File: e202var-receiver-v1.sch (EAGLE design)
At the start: 46 parts, among them P10 10k, Q1 BC237A/EQUIV, Q2 BC237A/EQUIV, U1 MC7809, U2 TLE2426, U3 LM386

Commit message: Added BOM.
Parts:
- removed JP1: 9V, SparkFun-Connectors:M02LOCK
- removed JP3: HEADPHONES, SparkFun-Connectors:AUDIO-JACK2.5MM
- added J1: 9V, SparkFun-Connectors:POWER_JACKPTH
- added J3: HEADPHONES, SparkFun-Connectors:AUDIO-JACK2KIT
- D3: value BLUE -> 3.2V BLUE
- renumbered HPF to JUMP1, JP2 to J2
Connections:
- net GND: now also J1.GND, J1.GNDBREAK, J3.RING, J3.RSH, J3.SLEEVE; no longer JP1.2, JP3.SLEEVE
- net N$1: now also J1.PWR; no longer JP1.1
- net N$25: now also J3.TIP, J3.TSH; no longer JP3.LEFT, JP3.RIGHT
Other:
- note added: "VOLUME"
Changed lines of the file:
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@@
 <parts>
 <part name="D1" library="max-viz" deviceset="S5BC-13" device="" value="1N4001"/>
-<part name="JP1" library="SparkFun-Connectors" deviceset="M02" device="LOCK" value="9V"/>
-<part name="JP2" library="SparkFun-Connectors" deviceset="M02" device="LOCK" value="ON/OFF"/>
+<part name="J2" library="SparkFun-Connectors" deviceset="M02" device="LOCK" value="ON/OFF"/>
 <part name="U1" library="SparkFun-PowerIC" deviceset="V_REG_LD1117VXX" device="" value="MC7809"/>
 <part name="D2" library="max-viz" deviceset="S5BC-13" device="" value="1N4001"/>
@@
 <part name="R4" library="SparkFun-Passives" deviceset="RESISTOR" device="EZ" value="3.3k"/>
 <part name="C16" library="SparkFun-Capacitors" deviceset="CAP" device="KIT" value="4.7n"/>
-<part name="HPF" library="SparkFun-Retired" deviceset="JUMPER-2" device="PTH_LOCK" value="HPF"/>
+<part name="JUMP1" library="SparkFun-Retired" deviceset="JUMPER-2" device="PTH_LOCK" value="HPF"/>
 <part name="U$7" library="max-viz" deviceset="GND" device=""/>
 <part name="U$8" library="max-viz" deviceset="GND" device=""/>
@@
 <part name="U$9" library="max-viz" deviceset="GND" device=""/>
 <part name="R12" library="SparkFun-Passives" deviceset="RESISTOR" device="EZ" value="2.2k"/>
-<part name="D3" library="SparkFun-LED" deviceset="LTE-302" device="" value="BLUE"/>
+<part name="D3" library="SparkFun-LED" deviceset="LTE-302" device="" value="3.2V BLUE"/>
 <part name="U$10" library="max-viz" deviceset="GND" device=""/>
 <part name="R9" library="SparkFun-Passives" deviceset="RESISTOR" device="EZ" value="33"/>
 <part name="R7" library="SparkFun-Passives" deviceset="RESISTOR" device="EZ" value="10"/>
 <part name="C9" library="SparkFun-Passives" deviceset="CAP" device="PTH1" value="100u"/>
-<part name="JP3" library="SparkFun-Connectors" deviceset="AUDIO-JACK" device="2.5MM" value="HEADPHONES"/>
+<part name="J3" library="SparkFun-Connectors" deviceset="AUDIO-JACK2" device="KIT" value="HEADPHONES"/>
 <part name="C10" library="SparkFun-Capacitors" deviceset="CAP" device="KIT" value="10n"/>
 <part name="U$11" library="max-viz" deviceset="GND" device=""/>
@@
 <part name="U$13" library="max-viz" deviceset="GND" device=""/>
 <part name="25-OCT-2015" library="max-viz" deviceset="FRAME-INFOBOX-WICKER" device="" value="VLF Natural Radio Receiver v1"/>
+<part name="J1" library="SparkFun-Connectors" deviceset="POWER_JACK" device="PTH" value="9V"/>
 </parts>
 <sheets>
@@
 <wire x1="238.76" y1="20.32" x2="238.76" y2="66.04" width="0.1524" layer="94"/>
 <frame x1="0" y1="0" x2="335.28" y2="182.88" columns="8" rows="5" layer="94"/>
+<text x="218.44" y="93.98" size="1.778" layer="97" rot="R90">VOLUME</text>
 </plain>
 <instances>
 <instance part="D1" gate="G$1" x="38.1" y="165.1" rot="R270"/>
-<instance part="JP1" gate="G$1" x="15.24" y="109.22" rot="MR180"/>
-<instance part="JP2" gate="G$1" x="15.24" y="129.54" rot="MR180"/>
+<instance part="J2" gate="G$1" x="15.24" y="129.54" rot="MR180"/>
 <instance part="U1" gate="G$1" x="63.5" y="149.86"/>
 <instance part="D2" gate="G$1" x="48.26" y="149.86" rot="R270"/>
@@
 <instance part="R4" gate="G$1" x="144.78" y="96.52"/>
 <instance part="C16" gate="G$1" x="137.16" y="83.82"/>
-<instance part="HPF" gate="A" x="147.32" y="86.36" rot="R270"/>
+<instance part="JUMP1" gate="A" x="147.32" y="86.36" rot="R270"/>
 <instance part="U$7" gate="G$1" x="154.94" y="129.54"/>
 <instance part="U$8" gate="G$1" x="162.56" y="99.06"/>
@@
 <instance part="R7" gate="G$1" x="276.86" y="91.44" rot="R90"/>
 <instance part="C9" gate="G$1" x="297.18" y="99.06" rot="R90"/>
-<instance part="JP3" gate="G$1" x="317.5" y="96.52" rot="R180"/>
+<instance part="J3" gate="G$1" x="317.5" y="96.52" rot="R180"/>
 <instance part="C10" gate="G$1" x="276.86" y="78.74"/>
 <instance part="U$11" gate="G$1" x="33.02" y="142.24"/>
@@
 <instance part="U$13" gate="G$1" x="241.3" y="119.38"/>
 <instance part="25-OCT-2015" gate="G$1" x="66.04" y="22.86"/>
+<instance part="J1" gate="G$1" x="20.32" y="101.6"/>
 </instances>
 <busses>
@@
 <net name="N$1" class="0">
 <segment>
-<pinref part="JP1" gate="G$1" pin="1"/>
 <wire x1="22.86" y1="109.22" x2="25.4" y2="109.22" width="0.1524" layer="91"/>
 <wire x1="25.4" y1="109.22" x2="25.4" y2="127" width="0.1524" layer="91"/>
-<pinref part="JP2" gate="G$1" pin="2"/>
+<pinref part="J2" gate="G$1" pin="2"/>
 <wire x1="25.4" y1="127" x2="22.86" y2="127" width="0.1524" layer="91"/>
+<pinref part="J1" gate="G$1" pin="PWR"/>
 </segment>
 </net>
 <net name="N$2" class="0">
 <segment>
-<pinref part="JP2" gate="G$1" pin="1"/>
+<pinref part="J2" gate="G$1" pin="1"/>
 <wire x1="22.86" y1="129.54" x2="25.4" y2="129.54" width="0.1524" layer="91"/>
 <wire x1="25.4" y1="129.54" x2="25.4" y2="165.1" width="0.1524" layer="91"/>
@@
 <pinref part="C16" gate="G$1" pin="2"/>
 <wire x1="137.16" y1="73.66" x2="137.16" y2="78.74" width="0.1524" layer="91"/>
-<pinref part="HPF" gate="A" pin="2"/>
+<pinref part="JUMP1" gate="A" pin="2"/>
 <wire x1="137.16" y1="78.74" x2="137.16" y2="81.28" width="0.1524" layer="91"/>
 <wire x1="137.16" y1="78.74" x2="147.32" y2="78.74" width="0.1524" layer="91"/>
@@
 <wire x1="114.3" y1="86.36" x2="114.3" y2="81.28" width="0.1524" layer="91"/>
 <junction x="114.3" y="86.36"/>
-<pinref part="JP1" gate="G$1" pin="2"/>
 <wire x1="22.86" y1="106.68" x2="25.4" y2="106.68" width="0.1524" layer="91"/>
-<wire x1="25.4" y1="106.68" x2="25.4" y2="81.28" width="0.1524" layer="91"/>
+<wire x1="25.4" y1="106.68" x2="25.4" y2="104.14" width="0.1524" layer="91"/>
+<wire x1="25.4" y1="104.14" x2="25.4" y2="81.28" width="0.1524" layer="91"/>
 <wire x1="114.3" y1="81.28" x2="68.58" y2="81.28" width="0.1524" layer="91"/>
 <pinref part="LAMP" gate="G$1" pin="2"/>
@@
 <wire x1="25.4" y1="81.28" x2="25.4" y2="78.74" width="0.1524" layer="91"/>
 <junction x="25.4" y="81.28"/>
+<pinref part="J1" gate="G$1" pin="GNDBREAK"/>
+<pinref part="J1" gate="G$1" pin="GND"/>
+<wire x1="22.86" y1="104.14" x2="25.4" y2="104.14" width="0.1524" layer="91"/>
+<junction x="25.4" y="104.14"/>
 </segment>
 <segment>
@@
 <wire x1="251.46" y1="83.82" x2="231.14" y2="83.82" width="0.1524" layer="91"/>
 <junction x="231.14" y="83.82"/>
-<pinref part="JP3" gate="G$1" pin="SLEEVE"/>
-<wire x1="312.42" y1="93.98" x2="309.88" y2="93.98" width="0.1524" layer="91"/>
-<wire x1="309.88" y1="93.98" x2="309.88" y2="68.58" width="0.1524" layer="91"/>
-<wire x1="309.88" y1="68.58" x2="276.86" y2="68.58" width="0.1524" layer="91"/>
+<wire x1="297.18" y1="91.44" x2="297.18" y2="68.58" width="0.1524" layer="91"/>
+<wire x1="297.18" y1="68.58" x2="276.86" y2="68.58" width="0.1524" layer="91"/>
 <wire x1="276.86" y1="68.58" x2="261.62" y2="68.58" width="0.1524" layer="91"/>
 <wire x1="261.62" y1="68.58" x2="251.46" y2="68.58" width="0.1524" layer="91"/>
@@
 <wire x1="276.86" y1="76.2" x2="276.86" y2="68.58" width="0.1524" layer="91"/>
 <junction x="276.86" y="68.58"/>
+<pinref part="J3" gate="G$1" pin="SLEEVE"/>
+<wire x1="312.42" y1="91.44" x2="302.26" y2="91.44" width="0.1524" layer="91"/>
+<pinref part="J3" gate="G$1" pin="RSH"/>
+<wire x1="302.26" y1="91.44" x2="297.18" y2="91.44" width="0.1524" layer="91"/>
+<wire x1="312.42" y1="96.52" x2="302.26" y2="96.52" width="0.1524" layer="91"/>
+<wire x1="302.26" y1="96.52" x2="302.26" y2="93.98" width="0.1524" layer="91"/>
+<junction x="302.26" y="91.44"/>
+<pinref part="J3" gate="G$1" pin="RING"/>
+<wire x1="302.26" y1="93.98" x2="302.26" y2="91.44" width="0.1524" layer="91"/>
+<wire x1="312.42" y1="93.98" x2="302.26" y2="93.98" width="0.1524" layer="91"/>
+<junction x="302.26" y="93.98"/>
 </segment>
 <segment>
@@
 <wire x1="137.16" y1="96.52" x2="137.16" y2="91.44" width="0.1524" layer="91"/>
 <pinref part="C16" gate="G$1" pin="1"/>
-<pinref part="HPF" gate="A" pin="1"/>
+<pinref part="JUMP1" gate="A" pin="1"/>
 <wire x1="137.16" y1="91.44" x2="137.16" y2="88.9" width="0.1524" layer="91"/>
 <wire x1="137.16" y1="91.44" x2="147.32" y2="91.44" width="0.1524" layer="91"/>
@@
 <segment>
 <pinref part="C9" gate="G$1" pin="2"/>
-<pinref part="JP3" gate="G$1" pin="LEFT"/>
-<wire x1="299.72" y1="99.06" x2="309.88" y2="99.06" width="0.1524" layer="91"/>
-<pinref part="JP3" gate="G$1" pin="RIGHT"/>
-<wire x1="309.88" y1="99.06" x2="312.42" y2="99.06" width="0.1524" layer="91"/>
-<wire x1="312.42" y1="96.52" x2="309.88" y2="96.52" width="0.1524" layer="91"/>
-<wire x1="309.88" y1="96.52" x2="309.88" y2="99.06" width="0.1524" layer="91"/>
-<junction x="309.88" y="99.06"/>
-</segment>
-</net>
+<wire x1="299.72" y1="99.06" x2="302.26" y2="99.06" width="0.1524" layer="91"/>
+<pinref part="J3" gate="G$1" pin="TSH"/>
+<wire x1="312.42" y1="99.06" x2="302.26" y2="99.06" width="0.1524" layer="91"/>
+<junction x="302.26" y="99.06"/>
+<pinref part="J3" gate="G$1" pin="TIP"/>
+<wire x1="312.42" y1="101.6" x2="302.26" y2="101.6" width="0.1524" layer="91"/>
+<wire x1="302.26" y1="101.6" x2="302.26" y2="99.06" width="0.1524" layer="91"/>
+</segment>
+</net>

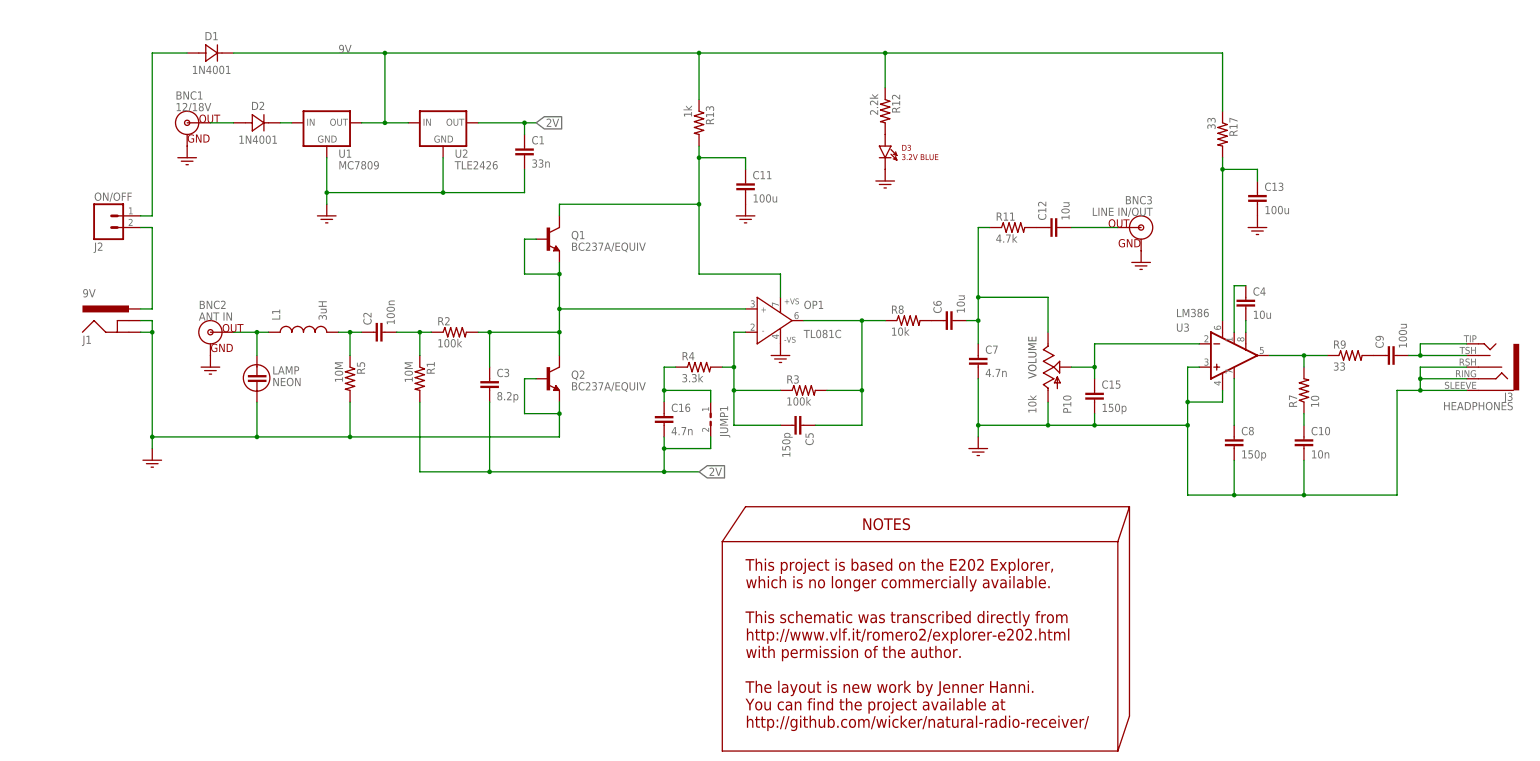
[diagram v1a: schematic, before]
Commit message: Added e202var library and clean schematic.
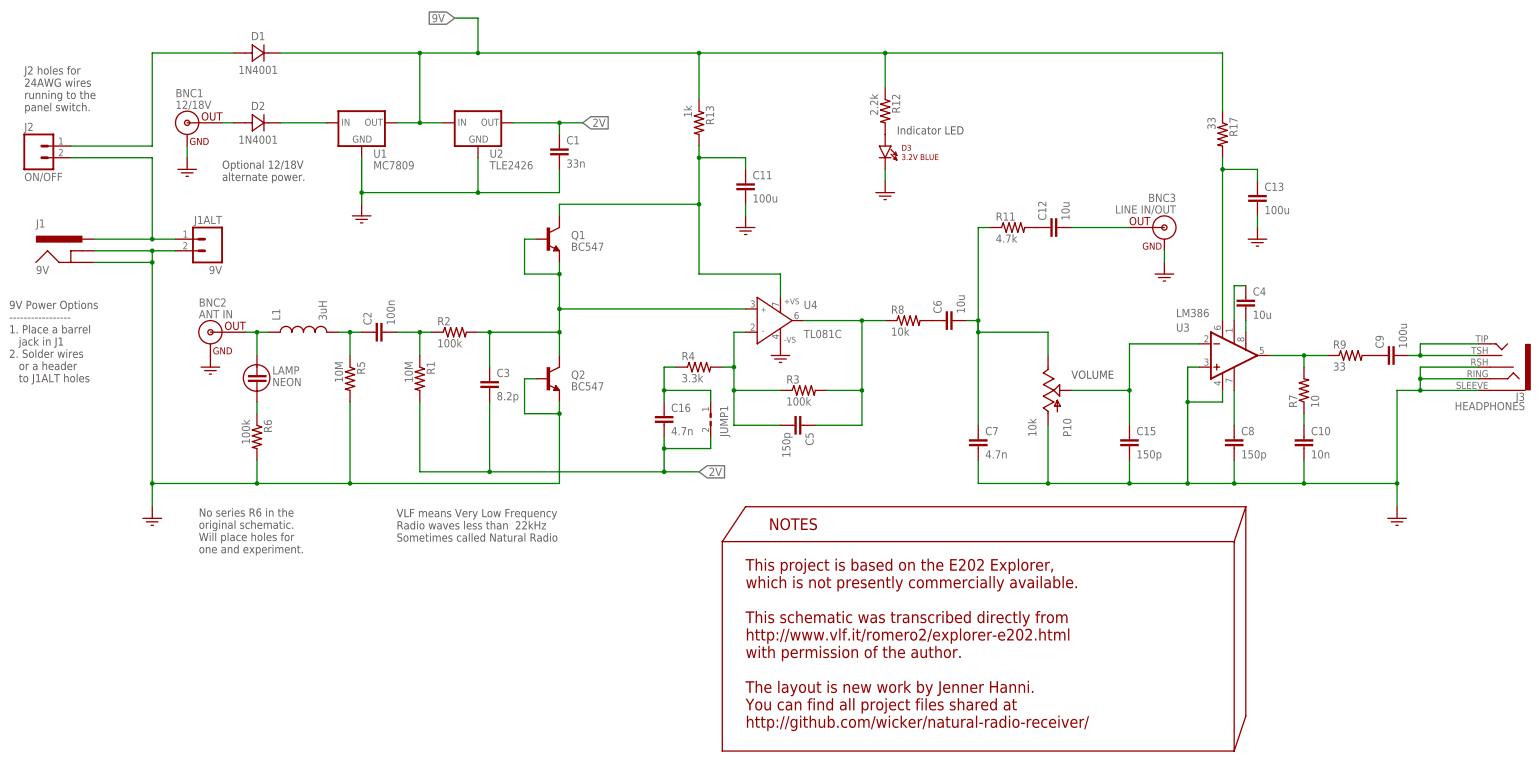
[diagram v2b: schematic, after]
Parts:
- removed OP1: TL081C, analog-devices:AD8597CP
- added J1ALT: 9V, e202var-receiver:CONN-2PIN
- added R6: 100k, e202var-receiver:RESISTOR
- added U4: TL081C, e202var-receiver:AMP-JFET-TL081CP
- BNC1, BNC2, BNC3: device SparkFun-Connectors:BNCPTH -> e202var-receiver:BNC-MOLEX-SD-73100
- C1, C16, C2, C3: device SparkFun-Capacitors:CAPKIT -> e202var-receiver:CAPACITOR5MM
- C10, C15, C5, C8: device SparkFun-Capacitors:CAPKIT -> e202var-receiver:CAPACITOR2.5MM
- C11, C13, C7, C9: device SparkFun-Passives:CAPPTH1 -> e202var-receiver:CAPACITOR5MM
- C12, C4, C6: device SparkFun-Passives:CAPPTH1 -> e202var-receiver:CAPACITOR2.5MM
- D1, D2: device max-viz:S5BC-13 -> e202var-receiver:DIODE
- D3: device SparkFun-LED:LTE-302 -> e202var-receiver:LED
- J1: device SparkFun-Connectors:POWER_JACKPTH -> e202var-receiver:JACK-POWER-BARREL
- J2: device SparkFun-Connectors:M02LOCK -> e202var-receiver:CONN-2PIN
- J3: device SparkFun-Connectors:AUDIO-JACK2KIT -> e202var-receiver:JACK-AUDIO
- JUMP1: device SparkFun-Retired:JUMPER-2PTH_LOCK -> e202var-receiver:JUMPER-SHUNT
- L1: device SparkFun-Passives:INDUCTORAXIAL-0.6 -> e202var-receiver:INDUCTOR
- LAMP: device max-viz:NEONLAMP -> e202var-receiver:LAMP-NEON
- P10: device SparkFun-Electromechanical:POT -> e202var-receiver:POT-P160KN-0QC15B10K
- Q1, Q2: value BC237A/EQUIV -> BC547; device SparkFun-DiscreteSemi:TRANSISTOR_NPNBC547 -> e202var-receiver:BJT-NPN
- R1, R11, R12, R13, R17, R2, R3, R4, R5, R7, R8, R9: device SparkFun-Passives:RESISTOREZ -> e202var-receiver:RESISTOR
- U1: device SparkFun-PowerIC:V_REG_LD1117VXX -> e202var-receiver:VOLTREG-MC7809
- U2: device SparkFun-PowerIC:V_REG_LD1117VXX -> e202var-receiver:VOLTREG-TLE2426
- U3: device SparkFun-AnalogIC:LM386 -> e202var-receiver:AMP-AUDIO-LM386
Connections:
- new net N$27: LAMP.2, R6.1
- net GND: now also D3.CATHODE, J1ALT.2, R6.2, U4.-VS; no longer D3.C, LAMP.2, OP1.-VS
- net N$1: now also J1ALT.1
- net N$13: now also U4.OUT; no longer OP1.OUT
- net N$22: now also D3.ANODE; no longer D3.A
- net N$4: now also U4.IN+; no longer OP1.IN+
- net N$6: now also U4.+VS; no longer OP1.+VS
- net N$8: now also U4.IN-; no longer OP1.IN-
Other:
- note added: "9V Power Options ----------------- 1. Place a barrel jack in J1 2. Solder wires or a header to J1ALT holes"
- note added: "Indicator LED"
- note added: "J2 holes for 24AWG wires running to the panel switch."
- note added: "No series R6 in the original schematic. Will place holes for one and experiment."
- note added: "Optional 12/18V alternate power."
- note added: "This project is based on the E202 Explorer, which is not presently commercially available. This schematic was transcribed directly from http://www.vlf.it/romero2/explorer-e202.html with permission of the author. The layout is new work by Jenner Hanni. You can find all project files shared at http://github.com/wicker/natural-radio-receiver/"
- note added: "VLF means Very Low Frequency Radio waves less than 22kHz Sometimes called Natural Radio"
- note removed: "This project is based on the E202 Explorer, which is no longer commercially available. This schematic was transcribed directly from http://www.vlf.it/romero2/explorer-e202.html with permission of the author. The layout is new work by Jenner Hanni. You can find the project available at http://github.com/wicker/natural-radio-receiver/"
- moved on the sheet: BNC3, C1, C15, C7, D1, D2, J1, J2, J3, P10, U1, U2
